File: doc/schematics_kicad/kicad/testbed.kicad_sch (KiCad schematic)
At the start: 0 parts

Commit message: tentacle v0.3
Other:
- title: Octoprobe: Infrastructure Tutorial -> Octoprobe: Testbed Tutorial
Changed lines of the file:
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@@
 	(paper "A4")
 	(title_block
-		(title "Octoprobe: Infrastructure Tutorial")
+		(title "Octoprobe: Testbed Tutorial")
 		(date "2024-07-16")
 		(company "Hans Märki, Märki Informatik")
@@
 		)
 		(instances
-			(project "infrastructure"
+			(project "testbed"
 				(path "/188054c4-74b7-429a-b3f5-c6f3151e27de"
 					(page "5")
@@
 		)
 		(instances
-			(project "infrastructure"
+			(project "testbed"
 				(path "/188054c4-74b7-429a-b3f5-c6f3151e27de"
 					(page "2")
@@
 		)
 		(instances
-			(project "infrastructure"
+			(project "testbed"
 				(path "/188054c4-74b7-429a-b3f5-c6f3151e27de"
 					(page "3")
@@
 		)
 		(instances
-			(project "infrastructure"
+			(project "testbed"
 				(path "/188054c4-74b7-429a-b3f5-c6f3151e27de"
 					(page "4")

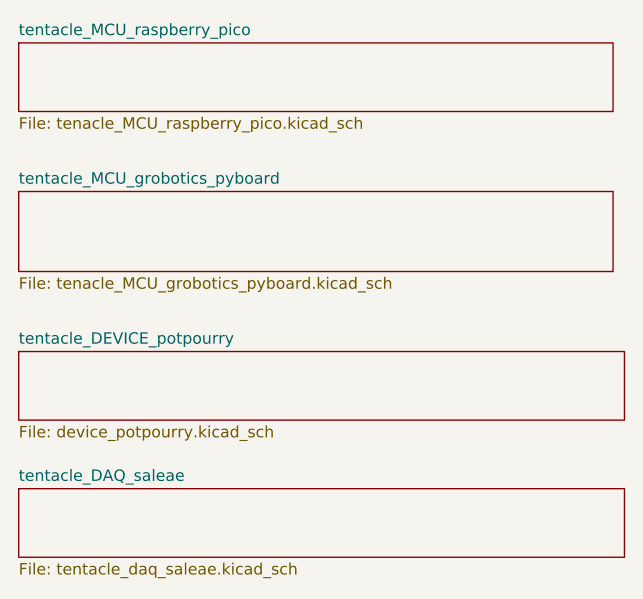
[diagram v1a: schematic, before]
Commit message: MCU names as in micropython-git
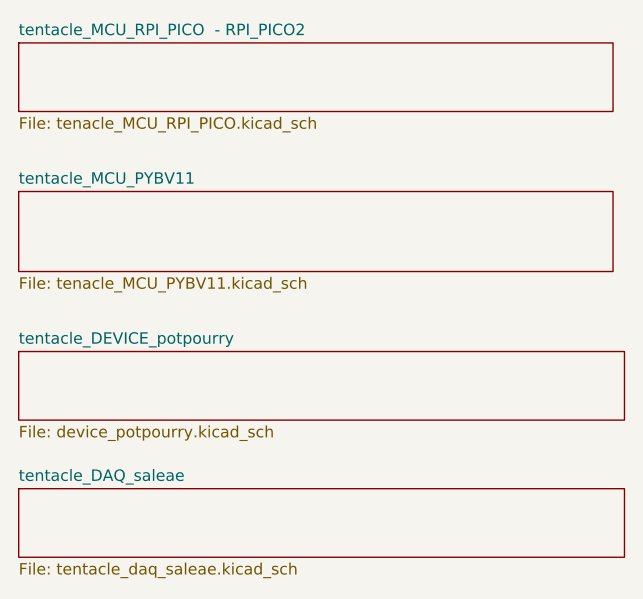
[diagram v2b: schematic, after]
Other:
- sheet tentacle_MCU_grobotics_pyboard renamed tentacle_MCU_PYBV11
- sheet tentacle_MCU_raspberry_pico renamed tentacle_MCU_RPI_PICO  - RPI_PICO2
- sheet tentacle_MCU_PYBV11: file tenacle_MCU_grobotics_pyboard.kicad_sch -> tenacle_MCU_PYBV11.kicad_sch
- sheet tentacle_MCU_RPI_PICO  - RPI_PICO2: file tenacle_MCU_raspberry_pico.kicad_sch -> tenacle_MCU_RPI_PICO.kicad_sch
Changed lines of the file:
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@@
 			(color 0 0 0 0.0000)
 		)
-		(property "Sheetname" "tentacle_MCU_raspberry_pico"
+		(property "Sheetname" "tentacle_MCU_RPI_PICO  - RPI_PICO2"
 			(at 36.83 32.3084 0)
 			(effects
@@
 			)
 		)
-		(property "Sheetfile" "tenacle_MCU_raspberry_pico.kicad_sch"
+		(property "Sheetfile" "tenacle_MCU_RPI_PICO.kicad_sch"
 			(at 36.83 41.2246 0)
 			(effects
@@
 			(color 0 0 0 0.0000)
 		)
-		(property "Sheetname" "tentacle_MCU_grobotics_pyboard"
+		(property "Sheetname" "tentacle_MCU_PYBV11"
 			(at 36.83 48.8184 0)
 			(effects
@@
 			)
 		)
-		(property "Sheetfile" "tenacle_MCU_grobotics_pyboard.kicad_sch"
+		(property "Sheetfile" "tenacle_MCU_PYBV11.kicad_sch"
 			(at 36.83 59.0046 0)
 			(effects
